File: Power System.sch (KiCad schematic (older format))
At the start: 22 parts, among them U13 splitter, U15 LMZ21701, U16 JST_Connector, U17 Switch_micromouse, U18 LMZ21701, U19 splitter

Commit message: generated a netlist
filled the teensy components with 0402 size untill i find out more info.
Starting to do PCB layout.
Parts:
- U16: footprint (none) -> Capacitors_SMD:C_0402
- U17: footprint switch:CK-JS102011SAQN_sm-spdt-switch -> micromouse:Switch_battery
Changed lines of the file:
@@
 F 0 "U16" H 1750 1775 39  0000 C CNN
 F 1 "JST_Connector" H 2000 1925 39  0000 C CNN
-F 2 "" H 2000 1675 39  0001 C CNN
+F 2 "Capacitors_SMD:C_0402" H 2000 1675 39  0001 C CNN
 F 3 "" H 1750 1775 39  0001 C CNN
 	1    2000 1675
@@
 F 0 "U17" H 3175 1875 39  0000 C CNN
 F 1 "Switch_micromouse" H 2825 2050 39  0000 C CNN
-F 2 "switch:CK-JS102011SAQN_sm-spdt-switch" H 2925 1700 39  0001 C CNN
+F 2 "micromouse:Switch_battery" H 2925 1700 39  0001 C CNN
 F 3 "" H 2925 1700 39  0001 C CNN
 	1    2925 1700

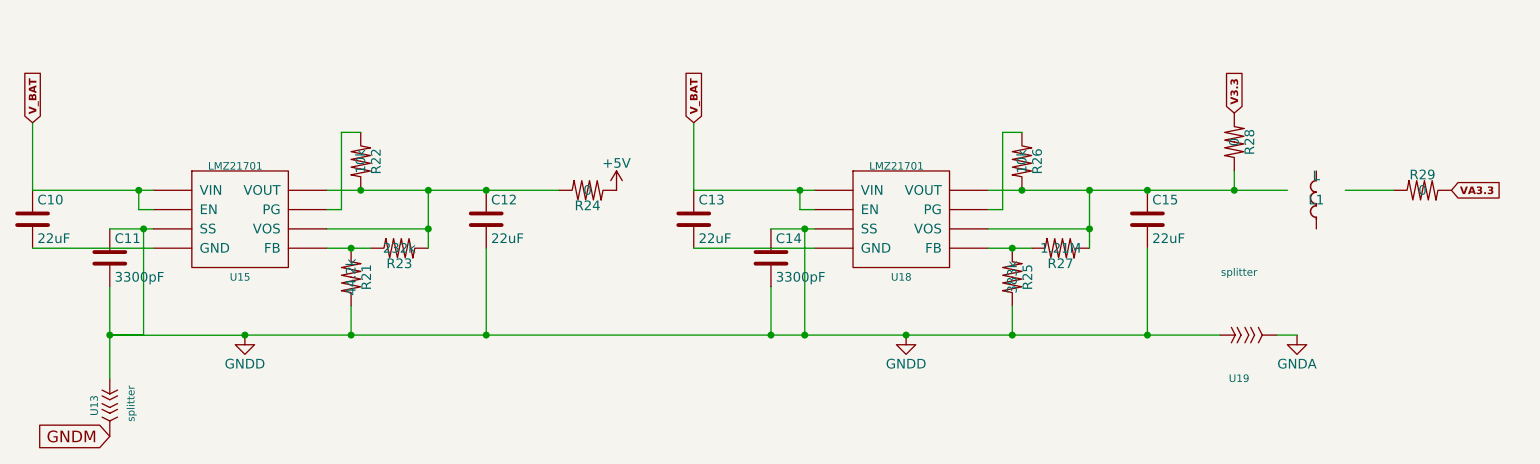
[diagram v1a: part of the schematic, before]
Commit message: Added MPU-6500
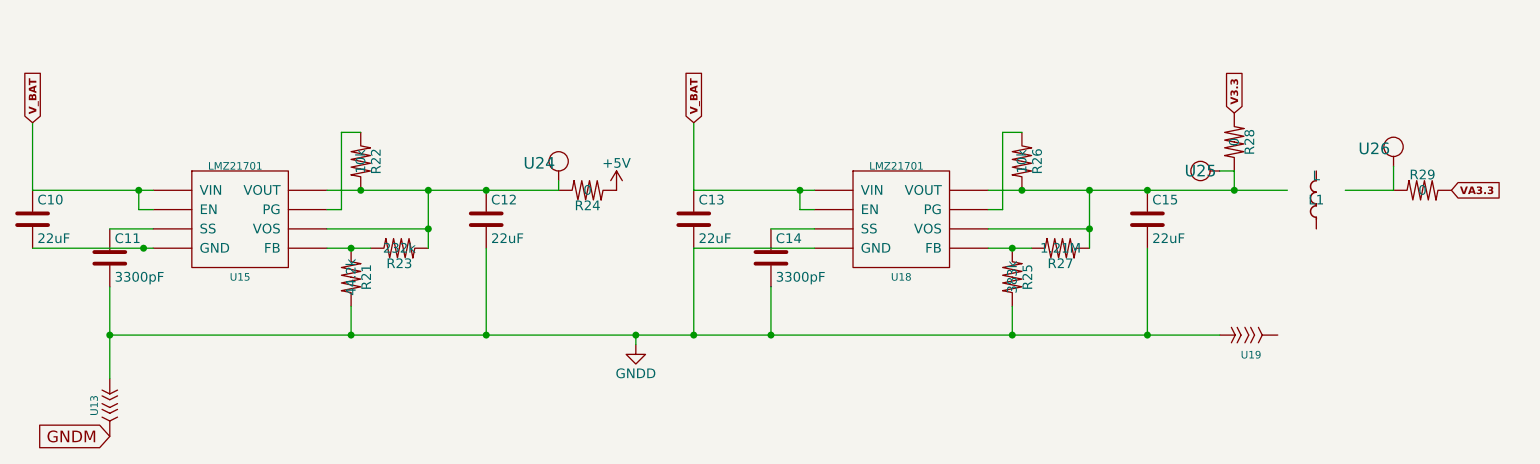
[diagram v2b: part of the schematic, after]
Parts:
- added U24, U25, U26: Test_Point, micromouse:Test_Point, symbol Test_Point
- C10, C12: footprint Capacitors_SMD:C_0603 -> Resistors_SMD:R_0805
- C11, C14: footprint Capacitors_SMD:C_0603 -> Capacitors_SMD:C_0402
- C13, C15: footprint Capacitors_SMD:C_0603 -> Capacitors_SMD:C_0805
- R21, R22, R23, R25, R26, R27: footprint Resistors_SMD:R_0603 -> Resistors_SMD:R_0402
- U18: footprint MicromouseFootprint:LMZ21701 -> micromouse:LMZ21701
- U19: footprint MicromouseFootprint:splitter -> micromouse:spliter
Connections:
- net labels removed: GNDA
- wire segments 44 -> 42

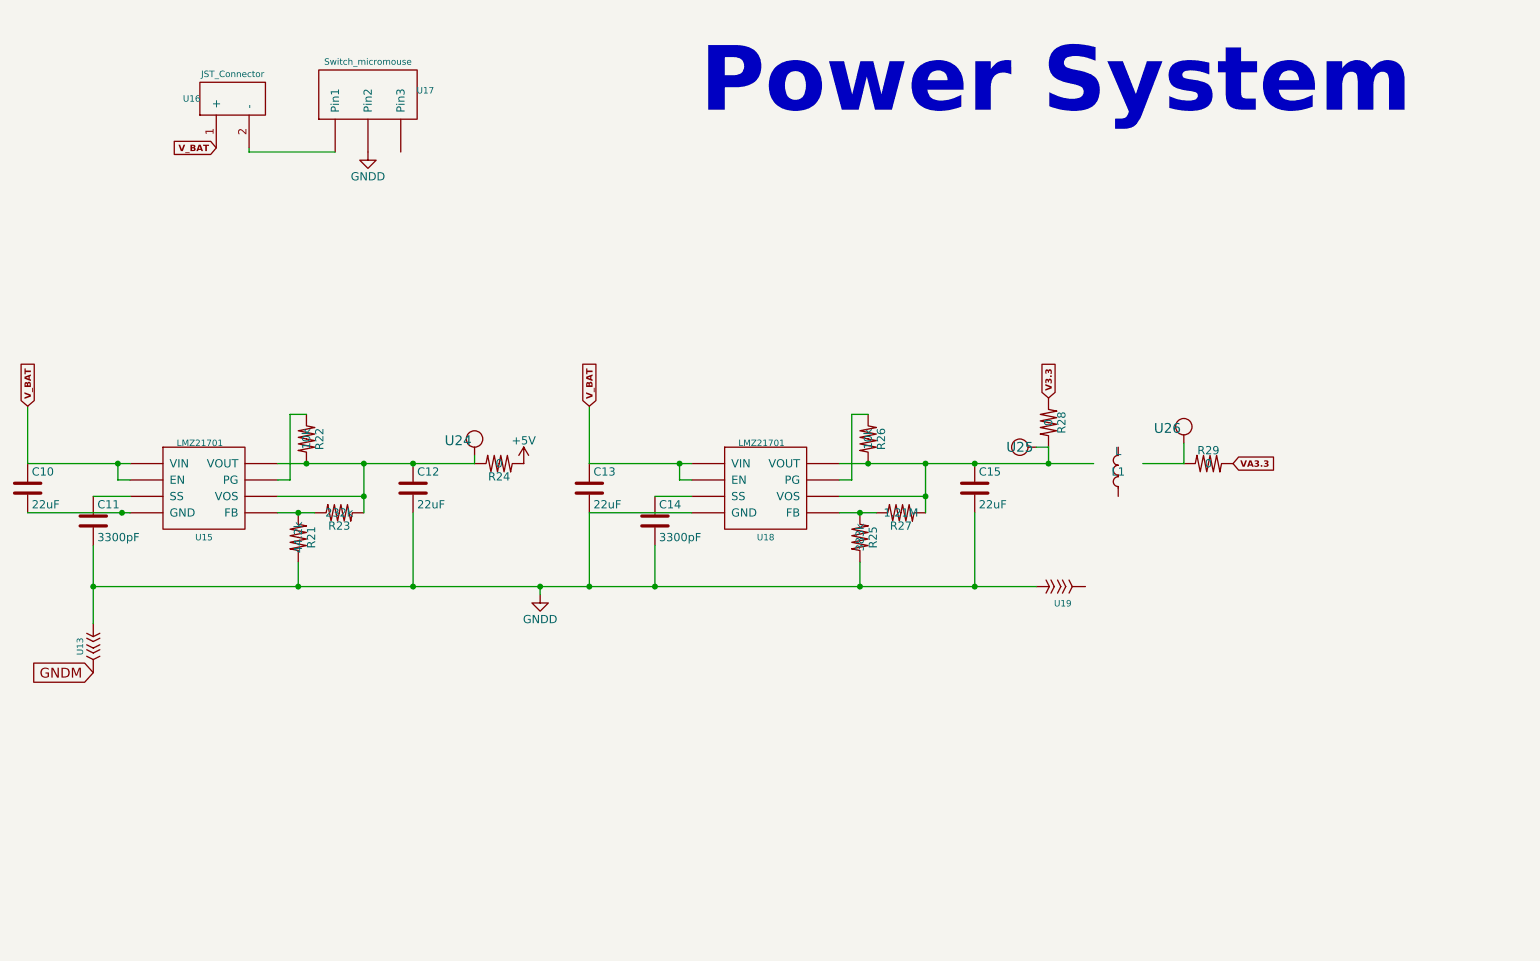
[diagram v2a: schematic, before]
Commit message: finished floor planning
-replaced the TC4427 and H brige by a single DRV8833 chip
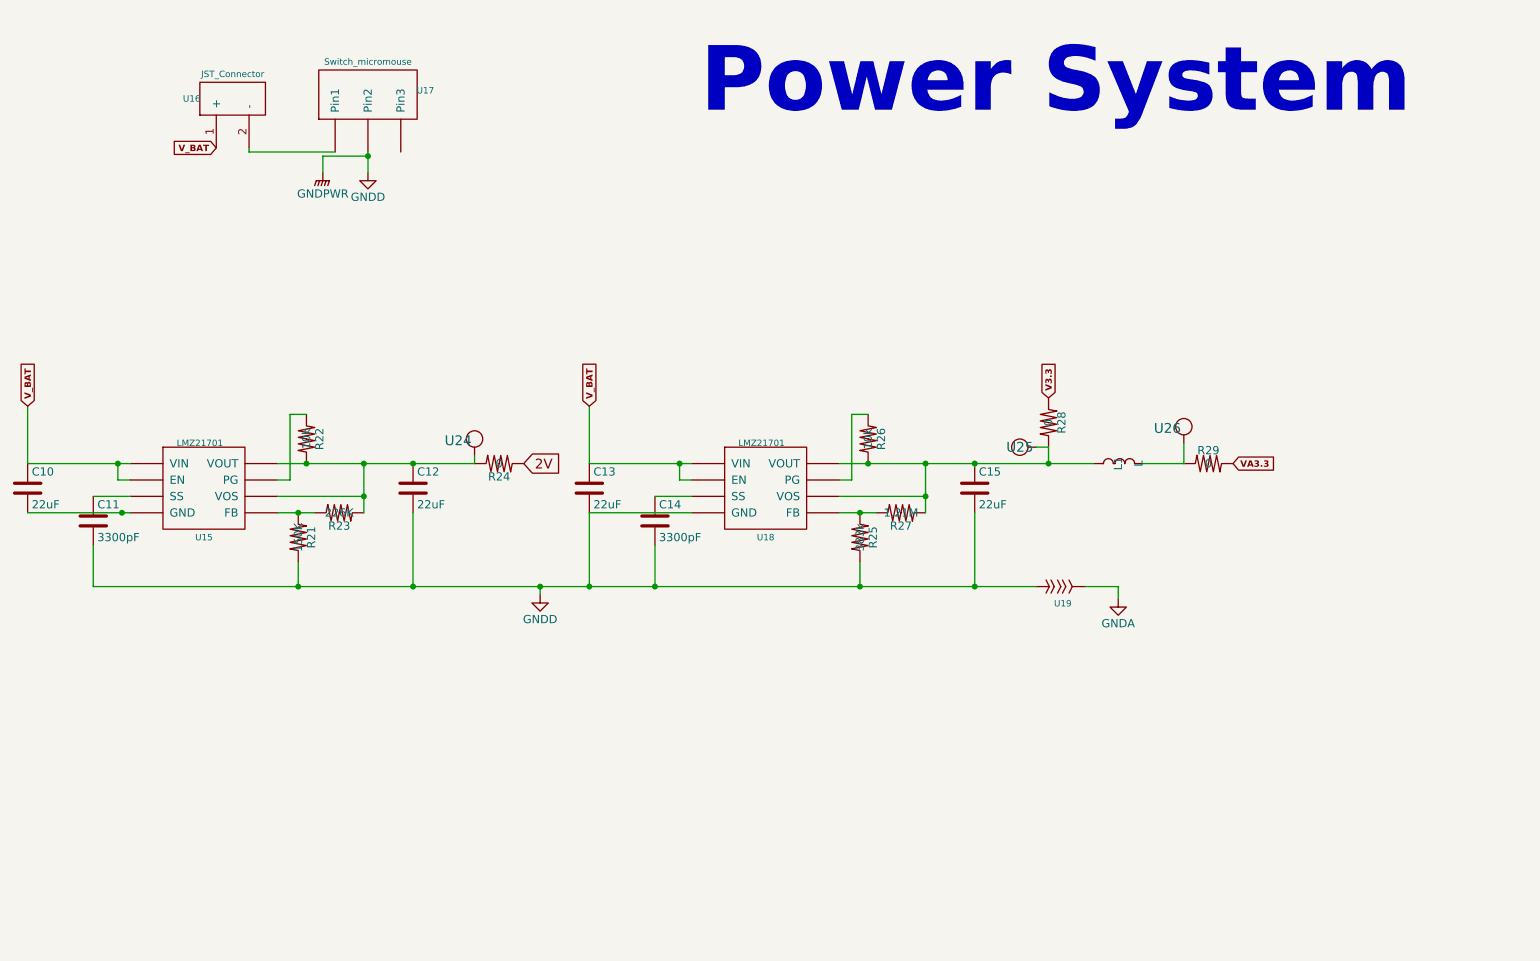
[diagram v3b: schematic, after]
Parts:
- removed U13: splitter, micromouse:spliter, symbol splitter
- C10: footprint Resistors_SMD:R_0805 -> micromouse:R_0805; manf# (none) -> JMK212BJ106KD-T
- C11: footprint Capacitors_SMD:C_0402 -> micromouse:C_0402; manf# (none) -> GRM033R70J332KA01D
- C12: footprint Resistors_SMD:R_0805 -> micromouse:R_0805; manf# (none) -> JMK212BJ226KG-T
- C13, C15: footprint Capacitors_SMD:C_0805 -> micromouse:C_0805
- C14: footprint Capacitors_SMD:C_0402 -> micromouse:C_0402
- R21: value 44.2k -> 150K; footprint Resistors_SMD:R_0402 -> micromouse:R_0402; manf# (none) -> ERJ-6ENF1503V
- R22, R25, R26, R27: footprint Resistors_SMD:R_0402 -> micromouse:R_0402
- R23: value 232k -> 226K; footprint Resistors_SMD:R_0402 -> micromouse:R_0402; manf# (none) -> CRCW0402226KFKED
- R24, R28, R29: footprint Resistors_SMD:R_0603 -> micromouse:R_0603
- U15: footprint MicromouseFootprint:LMZ21701 -> micromouse:LMZ21701
- U16: footprint Capacitors_SMD:C_0402 -> micromouse:JST_Connector
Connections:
- net labels added: 2V, GNDA, GNDPWR
- net labels removed: +5V, GNDM
- wire segments 42 -> 47
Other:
- moved on the sheet: L1
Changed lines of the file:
@@
 EESchema Schematic File Version 2
+LIBS:1_PJC-Sandbox
+LIBS:Micromouse1.2-rescue
+LIBS:Micromouse1.2-cache
+LIBS:74xgxx
+LIBS:74xx
+LIBS:ac-dc
+LIBS:actel
+LIBS:adc-dac
+LIBS:allegro
+LIBS:Altera
+LIBS:analog_devices
+LIBS:analog_switches
+LIBS:atmel
+LIBS:audio
+LIBS:battery_management
+LIBS:bbd
+LIBS:bosch
+LIBS:brooktre
+LIBS:cmos_ieee
+LIBS:cmos4000
+LIBS:conn
+LIBS:contrib
+LIBS:cypress
+LIBS:dc-dc
 LIBS:device
-LIBS:Micromouse
+LIBS:digital-audio
+LIBS:diode
+LIBS:display
+LIBS:dsp
+LIBS:elec-unifil
+LIBS:ESD_Protection
+LIBS:ftdi
+LIBS:gennum
+LIBS:graphic
+LIBS:hc11
+LIBS:intel
+LIBS:interface
+LIBS:ir
+LIBS:Lattice
+LIBS:leds
+LIBS:linear
+LIBS:logo
+LIBS:maxim
+LIBS:mechanical
+LIBS:memory
+LIBS:microchip
+LIBS:microchip_dspic33dsc
+LIBS:microchip_pic10mcu
+LIBS:microchip_pic12mcu
+LIBS:microchip_pic16mcu
+LIBS:microchip_pic18mcu
+LIBS:microchip_pic24mcu
+LIBS:microchip_pic32mcu
+LIBS:microcontrollers
+LIBS:modules
+LIBS:motor_drivers
+LIBS:motorola
+LIBS:motors
+LIBS:msp430
+LIBS:nordicsemi
+LIBS:nxp
+LIBS:nxp_armmcu
+LIBS:onsemi
+LIBS:opto
+LIBS:Oscillators
+LIBS:philips
 LIBS:power
+LIBS:Power_Management
+LIBS:powerint
+LIBS:pspice
+LIBS:references
+LIBS:regul
+LIBS:relays
+LIBS:rfcom
+LIBS:sensors
+LIBS:silabs
+LIBS:siliconi
+LIBS:stm8
+LIBS:stm32
+LIBS:supertex
+LIBS:switches
+LIBS:texas
+LIBS:transf
 LIBS:transistors
-LIBS:conn
-LIBS:linear
-LIBS:regul
-LIBS:74xx
-LIBS:cmos4000
-LIBS:adc-dac
-LIBS:memory
+LIBS:triac_thyristor
+LIBS:ttl_ieee
+LIBS:valves
+LIBS:video
+LIBS:wiznet
+LIBS:Worldsemi
+LIBS:Xicor
 LIBS:xilinx
-LIBS:microcontrollers
-LIBS:dsp
-LIBS:microchip
-LIBS:analog_switches
-LIBS:motorola
-LIBS:texas
-LIBS:intel
-LIBS:audio
-LIBS:interface
-LIBS:digital-audio
-LIBS:philips
-LIBS:display
-LIBS:cypress
-LIBS:siliconi
-LIBS:opto
-LIBS:atmel
-LIBS:contrib
-LIBS:valves
-LIBS:1_PJC-Sandbox
-LIBS:Micromouse1.2-cache
+LIBS:zetex
+LIBS:Zilog
 EELAYER 25 0
 EELAYER END
@@
 F 0 "C13" H 4200 4050 50  0000 L CNN
 F 1 "22uF" H 4200 3850 50  0000 L CNN
-F 2 "Capacitors_SMD:C_0805" H 4213 3800 50  0001 C CNN
+F 2 "micromouse:C_0805" H 4213 3800 50  0001 C CNN
 F 3 "" H 4175 3950 50  0001 C CNN
 	1    4175 3950
@@
 F 0 "C14" H 4600 4250 50  0000 L CNN
 F 1 "3300pF" H 4600 4050 50  0000 L CNN
-F 2 "Capacitors_SMD:C_0402" H 4613 4000 50  0001 C CNN
+F 2 "micromouse:C_0402" H 4613 4000 50  0001 C CNN
 F 3 "" H 4575 4150 50  0001 C CNN
 	1    4575 4150
@@
 F 0 "C15" H 6550 4050 50  0000 L CNN
 F 1 "22uF" H 6550 3850 50  0000 L CNN
-F 2 "Capacitors_SMD:C_0805" H 6563 3800 50  0001 C CNN
+F 2 "micromouse:C_0805" H 6563 3800 50  0001 C CNN
 F 3 "" H 6525 3950 50  0001 C CNN
 	1    6525 3950
@@
 F 0 "R27" V 6155 4100 50  0000 C CNN
 F 1 "1.21M" V 6075 4100 50  0000 C CNN
-F 2 "Resistors_SMD:R_0402" V 6005 4100 50  0001 C CNN
+F 2 "micromouse:R_0402" V 6005 4100 50  0001 C CNN
 F 3 "" H 6075 4100 50  0001 C CNN
 	1    6075 4100
@@
 F 0 "R25" V 5905 4250 50  0000 C CNN
 F 1 "383k" V 5825 4250 50  0000 C CNN
-F 2 "Resistors_SMD:R_0402" V 5755 4250 50  0001 C CNN
+F 2 "micromouse:R_0402" V 5755 4250 50  0001 C CNN
 F 3 "" H 5825 4250 50  0001 C CNN
 	1    5825 4250
@@
 F 0 "R26" V 5955 3650 50  0000 C CNN
 F 1 "10k" V 5875 3650 50  0000 C CNN
-F 2 "Resistors_SMD:R_0402" V 5805 3650 50  0001 C CNN
+F 2 "micromouse:R_0402" V 5805 3650 50  0001 C CNN
 F 3 "" H 5875 3650 50  0001 C CNN
 	1    5875 3650
@@
 F 0 "U15" H 1825 3550 39  0000 C CNN
 F 1 "LMZ21701" H 1800 4125 39  0000 C CNN
-F 2 "MicromouseFootprint:LMZ21701" H 1875 3600 39  0001 C CNN
+F 2 "micromouse:LMZ21701" H 1875 3600 39  0001 C CNN
 F 3 "" H 1875 3600 39  0001 C CNN
 F 4 "LMZ21701SILT" H 1875 3500 39  0001 C CNN "manf#"
@@
 F 0 "C10" H 775 4050 50  0000 L CNN
 F 1 "22uF" H 775 3850 50  0000 L CNN
-F 2 "Resistors_SMD:R_0805" H 788 3800 50  0001 C CNN
+F 2 "micromouse:R_0805" H 788 3800 50  0001 C CNN
 F 3 "" H 750 3950 50  0001 C CNN
+F 4 "JMK212BJ106KD-T" H 750 3950 60  0001 C CNN "manf#"
 	1    750  3950
 	1    0    0    -1
@@
 F 0 "C11" H 1175 4250 50  0000 L CNN
 F 1 "3300pF" H 1175 4050 50  0000 L CNN
-F 2 "Capacitors_SMD:C_0402" H 1188 4000 50  0001 C CNN
+F 2 "micromouse:C_0402" H 1188 4000 50  0001 C CNN
 F 3 "" H 1150 4150 50  0001 C CNN
+F 4 "GRM033R70J332KA01D" H 1150 4150 60  0001 C CNN "manf#"
 	1    1150 4150
-	1    0    0    -1
-$EndComp
-$Comp
-L C C12
-U 1 1 59465F7C
-P 3100 3950
-F 0 "C12" H 3125 4050 50  0000 L CNN
-F 1 "22uF" H 3125 3850 50  0000 L CNN
-F 2 "Resistors_SMD:R_0805" H 3138 3800 50  0001 C CNN
-F 3 "" H 3100 3950 50  0001 C CNN
-	1    3100 3950
 	1    0    0    -1
 $EndComp
@@
 P 2650 4100
 F 0 "R23" V 2730 4100 50  0000 C CNN
-F 1 "232k" V 2650 4100 50  0000 C CNN
-F 2 "Resistors_SMD:R_0402" V 2580 4100 50  0001 C CNN
+F 1 "226K" V 2650 4100 50  0000 C CNN
+F 2 "micromouse:R_0402" V 2580 4100 50  0001 C CNN
 F 3 "" H 2650 4100 50  0001 C CNN
+F 4 "CRCW0402226KFKED" V 2650 4100 60  0001 C CNN "manf#"
 	1    2650 4100
 	0    1    1    0
@@
 P 2400 4250
 F 0 "R21" V 2480 4250 50  0000 C CNN
-F 1 "44.2k" V 2400 4250 50  0000 C CNN
-F 2 "Resistors_SMD:R_0402" V 2330 4250 50  0001 C CNN
+F 1 "150K" V 2400 4250 50  0000 C CNN
+F 2 "micromouse:R_0402" V 2330 4250 50  0001 C CNN
 F 3 "" H 2400 4250 50  0001 C CNN
+F 4 "ERJ-6ENF1503V" V 2400 4250 60  0001 C CNN "manf#"
 	1    2400 4250
 	1    0    0    -1
@@
 F 0 "R22" V 2530 3650 50  0000 C CNN
 F 1 "10k" V 2450 3650 50  0000 C CNN
-F 2 "Resistors_SMD:R_0402" V 2380 3650 50  0001 C CNN
+F 2 "micromouse:R_0402" V 2380 3650 50  0001 C CNN
 F 3 "" H 2450 3650 50  0001 C CNN
 	1    2450 3650
@@
 V_BAT
 $Comp
-L +5V #PWR010
-U 1 1 59467C95
-P 3775 3800
-F 0 "#PWR010" H 3775 3650 50  0001 C CNN
-F 1 "+5V" H 3775 3940 50  0000 C CNN
-F 2 "" H 3775 3800 50  0001 C CNN
-F 3 "" H 3775 3800 50  0001 C CNN
-	1    3775 3800
-	1    0    0    -1
-$EndComp
-$Comp
 L L L1
 U 1 1 59467F19
-P 7400 3800
-F 0 "L1" V 7350 3800 50  0000 C CNN
-F 1 "L" V 7475 3800 50  0000 C CNN
-F 2 "Inductors_SMD:L_0603" H 7400 3800 50  0001 C CNN
-F 3 "" H 7400 3800 50  0001 C CNN
-	1    7400 3800
-	0    -1   -1   0
+P 7450 3800
+F 0 "L1" V 7400 3800 50  0000 C CNN
+F 1 "L" V 7525 3800 50  0000 C CNN
+F 2 "Inductors_SMD:L_0603" H 7450 3800 50  0001 C CNN
+F 3 "" H 7450 3800 50  0001 C CNN
+	1    7450 3800
+	1    0    0    -1
 $EndComp
 Text GLabel 8100 3800 2    39   Input ~ 8
@@
 F 0 "U16" H 1750 1775 39  0000 C CNN
 F 1 "JST_Connector" H 2000 1925 39  0000 C CNN
-F 2 "Capacitors_SMD:C_0402" H 2000 1675 39  0001 C CNN
+F 2 "micromouse:JST_Connector" H 2000 1675 39  0001 C CNN
 F 3 "" H 1750 1775 39  0001 C CNN
 	1    2000 1675
@@
 V_BAT
 $Comp
-L GNDD #PWR011
+L GNDD #PWR018
 U 1 1 59468675
-P 2825 1900
-F 0 "#PWR011" H 2825 1650 50  0001 C CNN
-F 1 "GNDD" H 2825 1750 50  0000 C CNN
-F 2 "" H 2825 1900 50  0001 C CNN
-F 3 "" H 2825 1900 50  0001 C CNN
-	1    2825 1900
-	1    0    0    -1
-$EndComp
-$Comp
-L splitter U13
-U 1 1 594B2CCC
-P 1150 4875
-F 0 "U13" H 1190 4795 39  0000 C CNN
-F 1 "splitter" H 1180 4985 39  0001 C CNN
-F 2 "micromouse:spliter" H 1150 4875 39  0001 C CNN
-F 3 "" H 1150 4875 39  0001 C CNN
-	1    1150 4875
-	0    1    1    0
+P 2825 2025
+F 0 "#PWR018" H 2825 1775 50  0001 C CNN
+F 1 "GNDD" H 2825 1875 50  0000 C CNN
+F 2 "" H 2825 2025 50  0001 C CNN
+F 3 "" H 2825 2025 50  0001 C CNN
+	1    2825 2025
+	1    0    0    -1
 $EndComp
 $Comp
@@
 F 0 "R24" V 3705 3800 50  0000 C CNN
 F 1 "0" V 3625 3800 50  0000 C CNN
-F 2 "Resistors_SMD:R_0603" V 3555 3800 50  0001 C CNN
+F 2 "micromouse:R_0603" V 3555 3800 50  0001 C CNN
 F 3 "" H 3625 3800 50  0001 C CNN
 	1    3625 3800
@@
 F 0 "R28" V 7055 3550 50  0000 C CNN
 F 1 "0" V 6975 3550 50  0000 C CNN
-F 2 "Resistors_SMD:R_0603" V 6905 3550 50  0001 C CNN
+F 2 "micromouse:R_0603" V 6905 3550 50  0001 C CNN
 F 3 "" H 6975 3550 50  0001 C CNN
 	1    6975 3550
@@
 F 0 "R29" V 8030 3800 50  0000 C CNN
 F 1 "0" V 7950 3800 50  0000 C CNN
-F 2 "Resistors_SMD:R_0603" V 7880 3800 50  0001 C CNN
+F 2 "micromouse:R_0603" V 7880 3800 50  0001 C CNN
 F 3 "" H 7950 3800 50  0001 C CNN
 	1    7950 3800
@@
 Text Notes 4850 1700 0    394  ~ 79
 Power System
-Text GLabel 1150 5075 0    60   Input ~ 0
-GNDM
 $Comp
 L Test_Point U25
@@
 $EndComp
 $Comp
-L GNDD #PWR012
+L GNDD #PWR019
 U 1 1 59A9B990
 P 3875 4600
-F 0 "#PWR012" H 3875 4350 50  0001 C CNN
+F 0 "#PWR019" H 3875 4350 50  0001 C CNN
 F 1 "GNDD" H 3875 4450 50  0000 C CNN
 F 2 "" H 3875 4600 50  0001 C CNN
@@
 	3475 3800 3475 3750
 Wire Wire Line
-	1150 4300 1150 4775
-Wire Wire Line
 	1150 4550 6900 4550
 Wire Wire Line
@@
 	2400 4400 2400 4550
 Connection ~ 2400 4550
-Connection ~ 1150 4550
 Wire Wire Line
 	3875 4600 3875 4550
@@
 Wire Wire Line
 	4175 4100 4175 4550
+Wire Wire Line
+	2825 1900 2825 2025
+$Comp
+L GNDPWR #PWR020
+U 1 1 59AE8307
+P 2550 2025
+F 0 "#PWR020" H 2550 1825 50  0001 C CNN
+F 1 "GNDPWR" H 2550 1895 50  0000 C CNN
+F 2 "" H 2550 1975 50  0001 C CNN
+F 3 "" H 2550 1975 50  0001 C CNN
+	1    2550 2025
+	1    0    0    -1
+$EndComp
+Wire Wire Line
+	2550 2025 2550 1925
+Wire Wire Line
+	2550 1925 2825 1925
+Connection ~ 2825 1925
+Wire Wire Line
+	1150 4300 1150 4550
+$Comp
+L GNDA #PWR021
+U 1 1 59AE9CB5
+P 7400 4625
+F 0 "#PWR021" H 7400 4375 50  0001 C CNN
+F 1 "GNDA" H 7400 4475 50  0000 C CNN
+F 2 "" H 7400 4625 50  0001 C CNN
+F 3 "" H 7400 4625 50  0001 C CNN
+	1    7400 4625
+	1    0    0    -1
+$EndComp
+Wire Wire Line
+	7200 4550 7400 4550
+Wire Wire Line
+	7400 4550 7400 4625
+Text GLabel 3775 3800 2    60   Input ~ 0
+2V
+$Comp
+L C C12
+U 1 1 59465F7C
+P 3100 3950
+F 0 "C12" H 3125 4050 50  0000 L CNN
+F 1 "22uF" H 3125 3850 50  0000 L CNN
+F 2 "micromouse:R_0805" H 3138 3800 50  0001 C CNN
+F 3 "" H 3100 3950 50  0001 C CNN
+F 4 "JMK212BJ226KG-T" H 3100 3950 60  0001 C CNN "manf#"
+	1    3100 3950
+	1    0    0    -1
+$EndComp
 $EndSCHEMATC
